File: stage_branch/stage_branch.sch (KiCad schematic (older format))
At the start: 1 part, among them P1 CONN_02X20

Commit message: Finished off the first page of the Stage Branch Decoding module.
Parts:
- removed P1: CONN_02X20, symbol CONN_02X20
- added P1: CONN_02X40, symbol CONN_02X40
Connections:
- net labels added: GEQZRO/, L15/, OVF/, PHS2/, PHS4, PHS4/, QC0/, SQ1/, SQEXT/, SUMA16/, SUMB16/, TL15, TMZ/, TOV/, TPZG/, TSGN/, TSGN2, TSGU/, UNF/, WL01/, WL02/, WL03/, WL04/, WL05/, WL06/, WL07/, WL08/, WL09/, WL10/, WL11/, WL12/, WL13/, WL14/, WL15/, WL16/
- wire segments 75 -> 171
- no-connect marks 8 -> 29

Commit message: Added page 2 of the Stage Branch Decoding module, and tied it into the rest of the system
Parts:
- removed P1: CONN_02X40, symbol CONN_02X40
- added P1: DIN_41612_128P, symbol DIN_41612_128P
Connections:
- net DVST: now also P1.63 (31B)
- net GEQZRO/: now also P1.65 (1C)
- net GND: now also P1.100 (4D), P1.101 (5D), P1.102 (6D), P1.103 (7D), P1.104 (8D), P1.105 (9D), P1.106 (10D), P1.107 (11D), P1.108 (12D), P1.109 (13D), P1.110 (14D), P1.111 (15D), P1.112 (16D), P1.113 (17D), P1.114 (18D), P1.115 (19D), P1.116 (20D), P1.117 (21D), P1.118 (22D), P1.119 (23D), P1.120 (24D), P1.121 (25D), P1.122 (26D), P1.123 (27D), P1.124 (28D), P1.125 (29D), P1.126 (30D), P1.127 (31D), P1.128 (32D), P1.32 (32A), P1.64 (32B), P1.96 (32C), P1.98 (2D), P1.99 (3D)
- net GOJAM: now also P1.1 (1A)
- net INKL: now also P1.68 (4C)
- net L15/: now also P1.69 (5C)
- net MTCSAI: now also P1.73 (9C)
- net NDR100/: now also P1.67 (3C)
- net OVF/: now also P1.49 (17B)
- net PHS2/: now also P1.2 (2A)
- net PHS3/: now also P1.3 (3A)
- net PHS4: now also P1.4 (4A)
- net PHS4/: now also P1.5 (5A)
- net QC0/: now also P1.23 (23A)
- net RSTSTG: now also P1.57 (25B)
- net SQ1/: now also P1.21 (21A)
- net SQEXT/: now also P1.27 (27A)
- net ST0/: now also P1.86 (22C)
- net ST1: now also P1.55 (23B)
- net ST1/: now also P1.87 (23C)
- net ST2: now also P1.56 (24B)
- net ST3/: now also P1.89 (25C)
- net ST4/: now also P1.90 (26C)
- net STD2: now also P1.88 (24C)
- net STRTFC: now also P1.31 (31A)
- net SUMA16/: now also P1.51 (19B)
- net SUMB16/: now also P1.52 (20B)
- net T01: now also P1.6 (6A)
- net T03: now also P1.7 (7A)
- net T12/: now also P1.19 (19A)
- net TL15: now also P1.70 (6C)
- net TMZ/: now also P1.58 (26B)
- net TOV/: now also P1.59 (27B)
- net TPZG/: now also P1.62 (30B)
- net TSGN/: now also P1.60 (28B)
- net TSGU/: now also P1.61 (29B)
- net UNF/: now also P1.50 (18B)
- net VCC: now also P1.97 (1D)
- net WL01/: now also P1.48 (16B)
- net WL02/: now also P1.47 (15B)
- net WL03/: now also P1.46 (14B)
- net WL04/: now also P1.45 (13B)
- net WL05/: now also P1.44 (12B)
- net WL06/: now also P1.43 (11B)
- net WL07/: now also P1.42 (10B)
- net WL08/: now also P1.41 (9B)
- net WL09/: now also P1.40 (8B)
- net WL10/: now also P1.39 (7B)
- net WL11/: now also P1.38 (6B)
- net WL12/: now also P1.37 (5B)
- net WL13/: now also P1.36 (4B)
- net WL14/: now also P1.35 (3B)
- net WL15/: now also P1.34 (2B)
- net WL16/: now also P1.33 (1B)
- net XB7/: now also P1.72 (8C)
- net XT1/: now also P1.71 (7C)
- new net 5XP4: P1.95 (31C)
- new net 7XP14: P1.85 (21C)
- new net BR1B2B: P1.92 (28C)
- new net BR2/: P1.91 (27C)
- new net EXST0/: P1.53 (21B)
- new net EXST1/: P1.54 (22B)
- new net IC12: P1.78 (14C)
- new net IC13: P1.79 (15C)
- new net IC15: P1.80 (16C)
- new net KRPT: P1.93 (29C)
- new net MP0/: P1.74 (10C)
- new net MP1: P1.75 (11C)
- new net MP3/: P1.77 (13C)
- new net MP3A: P1.76 (12C)
- new net QC1/: P1.24 (24A)
- new net QC2/: P1.25 (25A)
- new net QC3/: P1.26 (26A)
- new net RSM3: P1.82 (18C)
- new net RSM3/: P1.83 (19C)
- new net RXOR0: P1.94 (30C)
- new net SQ0/: P1.20 (20A)
- new net SQ2/: P1.22 (22A)
- new net SQR10: P1.28 (28A)
- new net SQR10/: P1.29 (29A)
- new net SQR12/: P1.30 (30A)
- new net STORE1/: P1.84 (20C)
- new net T01/: P1.8 (8A)
- new net T02/: P1.9 (9A)
- new net T03/: P1.10 (10A)
- new net T04/: P1.11 (11A)
- new net T05/: P1.12 (12A)
- new net T06/: P1.13 (13A)
- new net T07/: P1.14 (14A)
- new net T08/: P1.15 (15A)
- new net T09/: P1.16 (16A)
- new net T10/: P1.17 (17A)
- new net T11/: P1.18 (18A)
- new net TRSM: P1.66 (2C)
- new net TS0/: P1.81 (17C)
- no-connect marks 29 -> 78

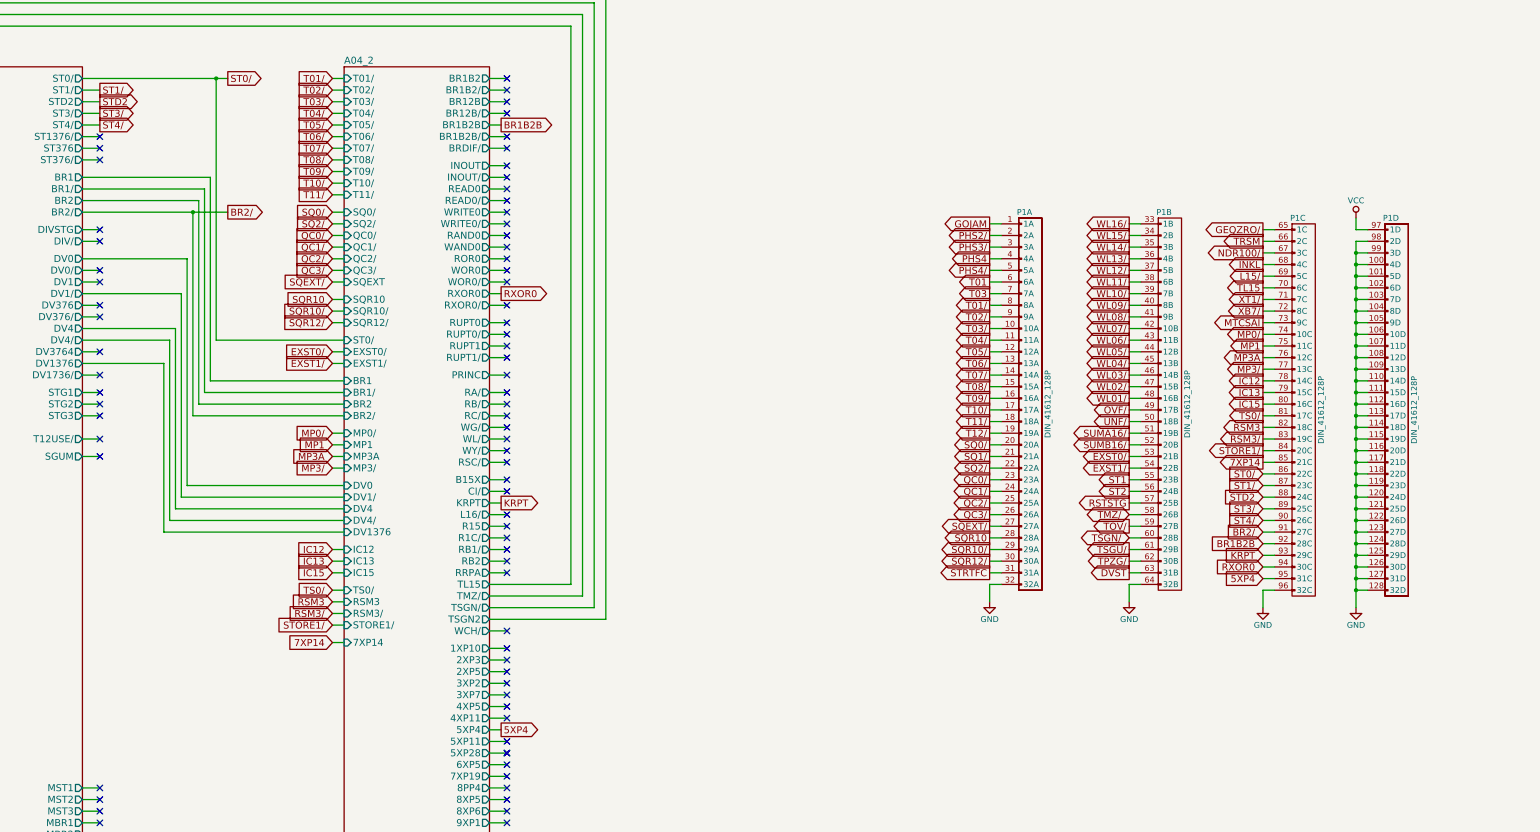
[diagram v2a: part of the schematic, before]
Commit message: Finished the second page of crosspoint generator 1 and tied it into the rest of the system.
Turns out most documentation online is wrong, and block 2 modules have 276 pins per module to the backplane, rather than the 140-144 that is quoted everywhere (those are block 1 figures). Instead of dealing with connector selection again, I opted to just add another row to the '128-pin' connector. I'll fix that more properly later
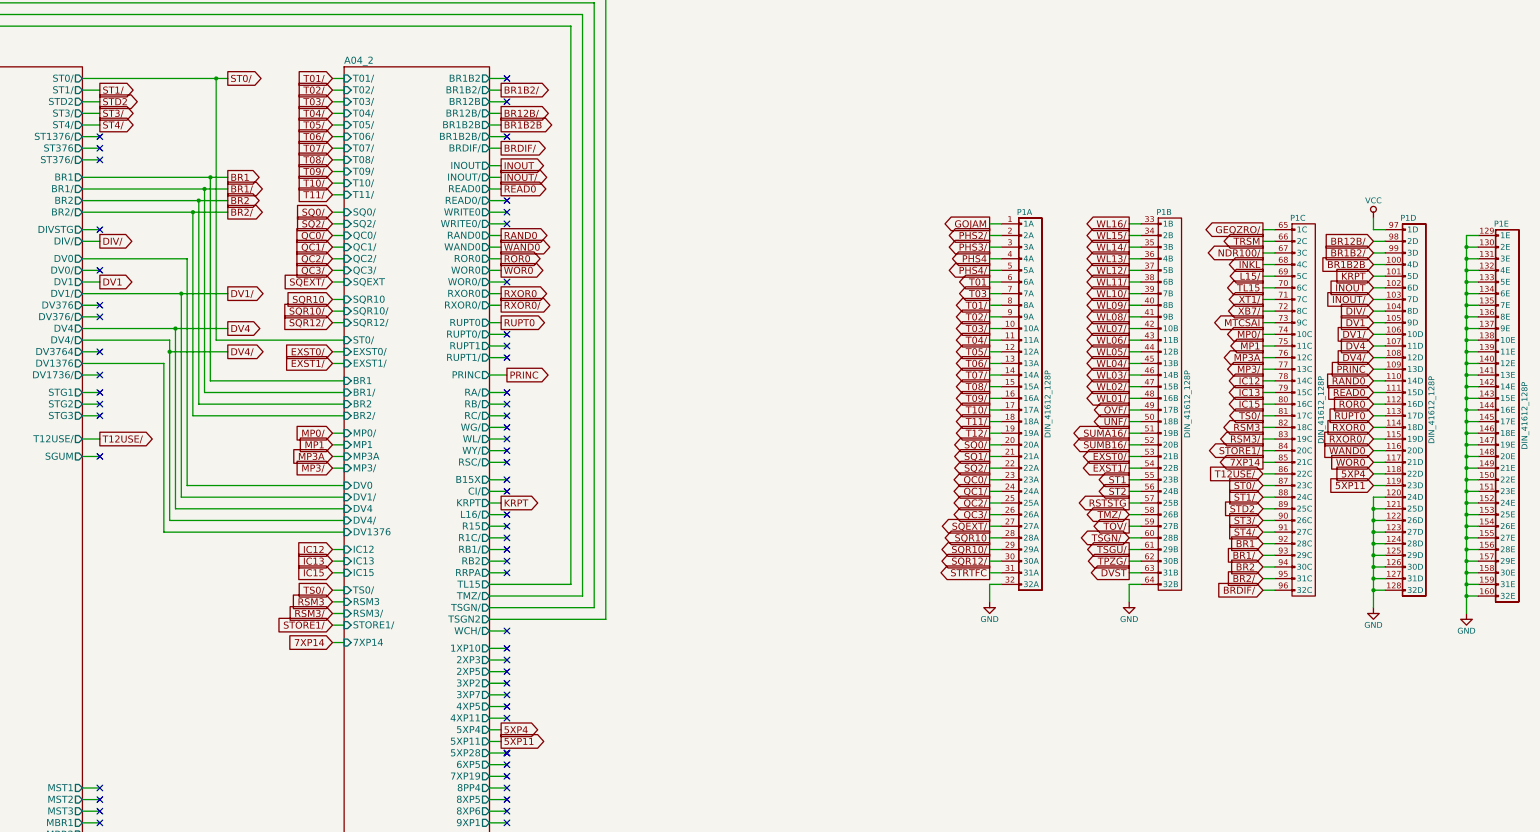
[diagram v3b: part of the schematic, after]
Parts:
- added unit 5 of P1
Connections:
- net 5XP4: now also P1.118 (22D); no longer P1.95 (31C)
- net BR1B2B: now also P1.100 (4D); no longer P1.92 (28C)
- net BR2/: now also P1.95 (31C); no longer P1.91 (27C)
- net GND: now also P1.129 (1E), P1.130 (2E), P1.131 (3E), P1.132 (4E), P1.133 (5E), P1.134 (6E), P1.135 (7E), P1.136 (8E), P1.137 (9E), P1.138 (10E), P1.139 (11E), P1.140 (12E), P1.141 (13E), P1.142 (14E), P1.143 (15E), P1.144 (16E), P1.145 (17E), P1.146 (18E), P1.147 (19E), P1.148 (20E), P1.149 (21E), P1.150 (22E), P1.151 (23E), P1.152 (24E), P1.153 (25E), P1.154 (26E), P1.155 (27E), P1.156 (28E), P1.157 (29E), P1.158 (30E), P1.159 (31E), P1.160 (32E); no longer P1.100 (4D), P1.101 (5D), P1.102 (6D), P1.103 (7D), P1.104 (8D), P1.105 (9D), P1.106 (10D), P1.107 (11D), P1.108 (12D), P1.109 (13D), P1.110 (14D), P1.111 (15D), P1.112 (16D), P1.113 (17D), P1.114 (18D), P1.115 (19D), P1.116 (20D), P1.117 (21D), P1.118 (22D), P1.119 (23D), P1.96 (32C), P1.98 (2D), P1.99 (3D)
- net KRPT: now also P1.101 (5D); no longer P1.93 (29C)
- net RXOR0: now also P1.114 (18D); no longer P1.94 (30C)
- net ST0/: now also P1.87 (23C); no longer P1.86 (22C)
- net ST1/: now also P1.88 (24C); no longer P1.87 (23C)
- net ST3/: now also P1.90 (26C); no longer P1.89 (25C)
- net ST4/: now also P1.91 (27C); no longer P1.90 (26C)
- net STD2: now also P1.89 (25C); no longer P1.88 (24C)
- new net 5XP11: P1.119 (23D)
- new net BR1: P1.92 (28C)
- new net BR1/: P1.93 (29C)
- new net BR12B/: P1.98 (2D)
- new net BR1B2/: P1.99 (3D)
- new net BR2: P1.94 (30C)
- new net BRDIF/: P1.96 (32C)
- new net DIV/: P1.104 (8D)
- new net DV1: P1.105 (9D)
- new net DV1/: P1.106 (10D)
- new net DV4: P1.107 (11D)
- new net DV4/: P1.108 (12D)
- new net INOUT: P1.102 (6D)
- new net INOUT/: P1.103 (7D)
- new net PRINC: P1.109 (13D)
- new net RAND0: P1.110 (14D)
- new net READ0: P1.111 (15D)
- new net ROR0: P1.112 (16D)
- new net RUPT0: P1.113 (17D)
- new net RXOR0/: P1.115 (19D)
- new net T12USE/: P1.86 (22C)
- new net WAND0: P1.116 (20D)
- new net WOR0: P1.117 (21D)
- no-connect marks 78 -> 61
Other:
- moved on the sheet: P1D

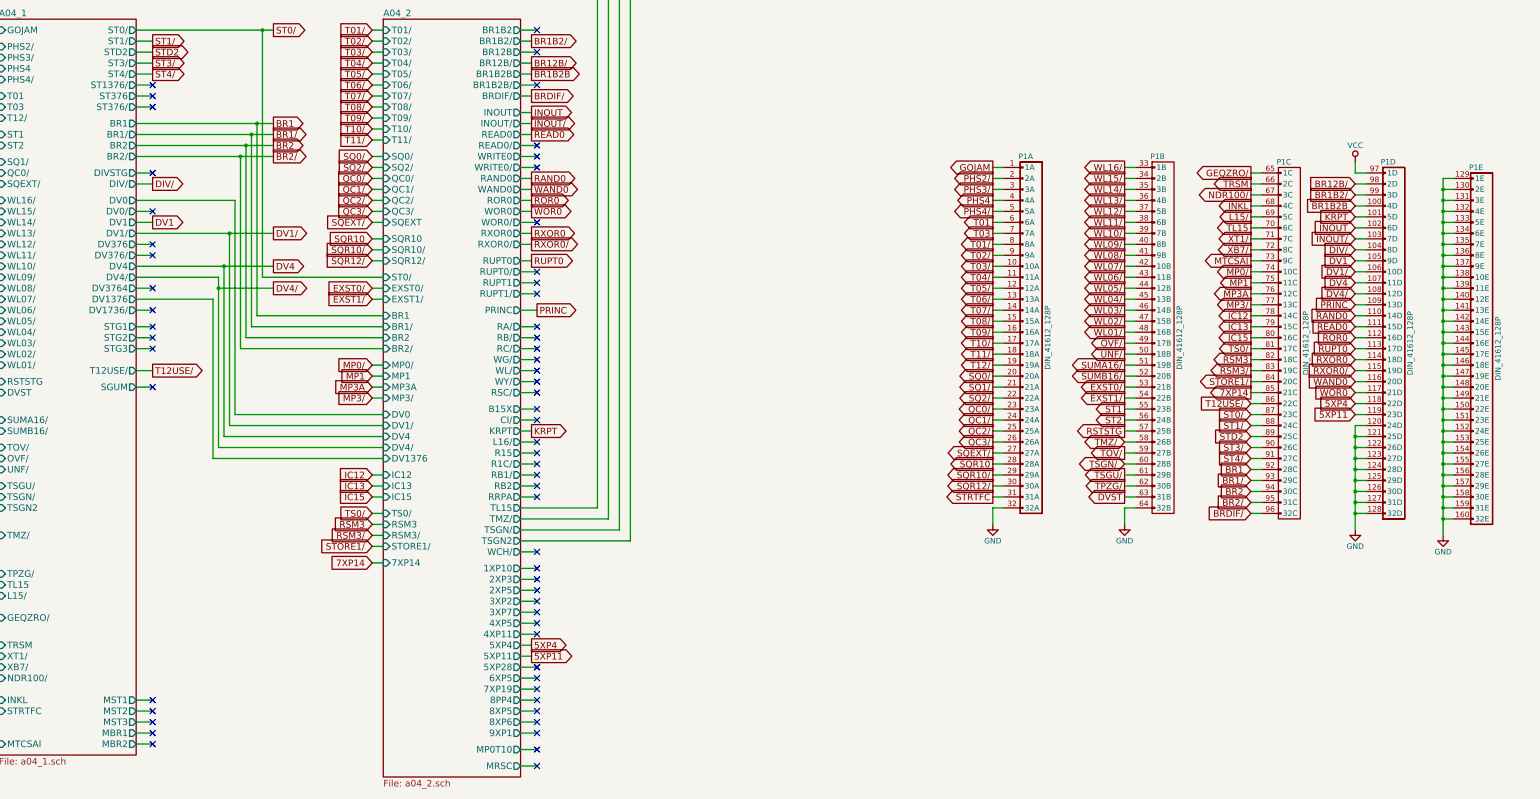
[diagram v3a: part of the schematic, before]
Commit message: Tied in module 6 and corrected a handful of naming/routing errors... most notably some missing gates from A06-1
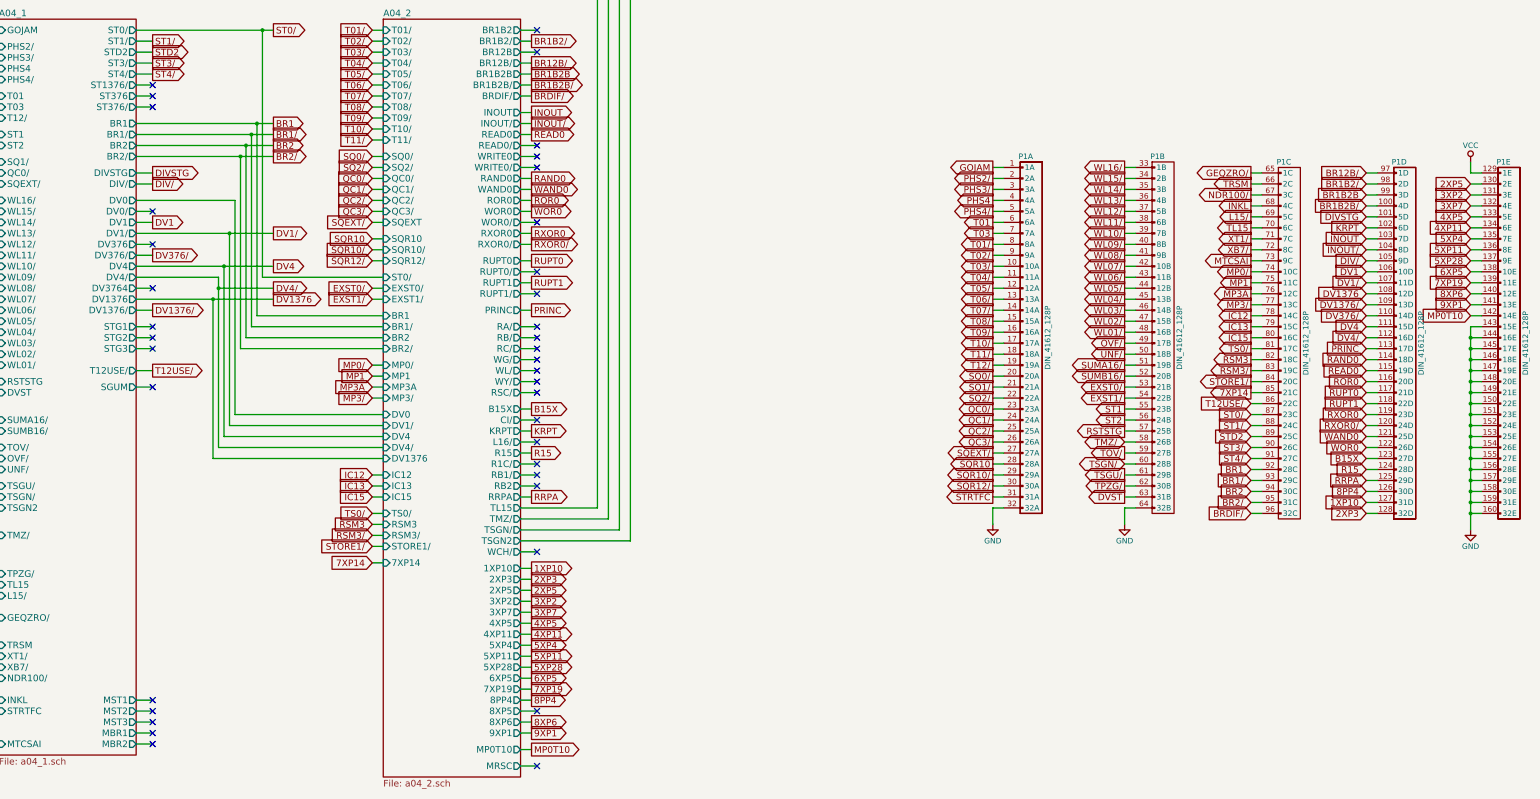
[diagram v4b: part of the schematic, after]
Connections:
- net 5XP11: now also P1.136 (8E); no longer P1.119 (23D)
- net 5XP4: now also P1.135 (7E); no longer P1.118 (22D)
- net BR12B/: now also P1.97 (1D); no longer P1.98 (2D)
- net BR1B2/: now also P1.98 (2D); no longer P1.99 (3D)
- net BR1B2B: now also P1.99 (3D); no longer P1.100 (4D)
- net DIV/: now also P1.105 (9D); no longer P1.104 (8D)
- net DV1: now also P1.106 (10D); no longer P1.105 (9D)
- net DV1/: now also P1.107 (11D); no longer P1.106 (10D)
- net DV4: now also P1.111 (15D); no longer P1.107 (11D)
- net DV4/: now also P1.112 (16D); no longer P1.108 (12D)
- net GND: no longer P1.120 (24D), P1.121 (25D), P1.122 (26D), P1.123 (27D), P1.124 (28D), P1.125 (29D), P1.126 (30D), P1.127 (31D), P1.128 (32D), P1.129 (1E), P1.130 (2E), P1.131 (3E), P1.132 (4E), P1.133 (5E), P1.134 (6E), P1.135 (7E), P1.136 (8E), P1.137 (9E), P1.138 (10E), P1.139 (11E), P1.140 (12E), P1.141 (13E), P1.142 (14E)
- net INOUT: now also P1.103 (7D); no longer P1.102 (6D)
- net INOUT/: now also P1.104 (8D); no longer P1.103 (7D)
- net KRPT: now also P1.102 (6D); no longer P1.101 (5D)
- net PRINC: now also P1.113 (17D); no longer P1.109 (13D)
- net RAND0: now also P1.114 (18D); no longer P1.110 (14D)
- net READ0: now also P1.115 (19D); no longer P1.111 (15D)
- net ROR0: now also P1.116 (20D); no longer P1.112 (16D)
- net RUPT0: now also P1.117 (21D); no longer P1.113 (17D)
- net RXOR0: now also P1.119 (23D); no longer P1.114 (18D)
- net RXOR0/: now also P1.120 (24D); no longer P1.115 (19D)
- net VCC: now also P1.129 (1E); no longer P1.97 (1D)
- net WAND0: now also P1.121 (25D); no longer P1.116 (20D)
- net WOR0: now also P1.122 (26D); no longer P1.117 (21D)
- new net 1XP10: P1.127 (31D)
- new net 2XP3: P1.128 (32D)
- new net 2XP5: P1.130 (2E)
- new net 3XP2: P1.131 (3E)
- new net 3XP7: P1.132 (4E)
- new net 4XP11: P1.134 (6E)
- new net 4XP5: P1.133 (5E)
- new net 5XP28: P1.137 (9E)
- new net 6XP5: P1.138 (10E)
- new net 7XP19: P1.139 (11E)
- new net 8PP4: P1.126 (30D)
- new net 8XP6: P1.140 (12E)
- new net 9XP1: P1.141 (13E)
- new net B15X: P1.123 (27D)
- new net BR1B2B/: P1.100 (4D)
- new net DIVSTG: P1.101 (5D)
- new net DV1376: P1.108 (12D)
- new net DV1376/: P1.109 (13D)
- new net DV376/: P1.110 (14D)
- new net MP0T10: P1.142 (14E)
- new net R15: P1.124 (28D)
- new net RRPA: P1.125 (29D)
- new net RUPT1: P1.118 (22D)
- no-connect marks 61 -> 38
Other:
- moved on the sheet: P1D, P1E
